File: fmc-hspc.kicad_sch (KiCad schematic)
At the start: 36 parts, among them J18 ASP-184329-01_mounting_holes_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

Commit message: Loclib
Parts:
- C296: footprint antmicro-footprints:0402-cap_EIA -> K410T-devboard-footprints:0402-cap_EIA; symbol antmicroCapacitors0402:C_100n_0402_EIA -> K410T-devboard:C_100n_0402_EIA
- C297: footprint antmicro-footprints:1206-cap -> K410T-devboard-footprints:1206-cap; symbol antmicroCapacitorsmisc:C_47u_16V_1206 -> K410T-devboard:C_47u_16V_1206
- C298, C299, C300, C301, C302, C303, C304, C305, C306, C307, C308, C309, C310, C311, C312, C313: footprint antmicro-footprints:0402-cap -> K410T-devboard-footprints:0402-cap; symbol antmicroCapacitors0402:C_100n_0402 -> K410T-devboard:C_100n_0402
- D32: footprint antmicro-footprints:Nexperia_SOD128 -> K410T-devboard-footprints:Nexperia_SOD128; symbol antmicroDiodesRectifiersSingle:PMEG3050EP,115 -> K410T-devboard:PMEG3050EP,115
- J18: footprint antmicro-footprints:ASP-184329-01_mounting_holes -> K410T-devboard-footprints:ASP-184329-01_mounting_holes; symbol antmicroFMC+Connectors:ASP-184329-01_mounting_holes_FMCPinout -> K410T-devboard:ASP-184329-01_mounting_holes_FMCPinout
- R264: footprint antmicro-footprints:0402-res -> K410T-devboard-footprints:0402-res; symbol antmicroResistors0402:R_100k_0402 -> K410T-devboard:R_100k_0402
- R265, R266: footprint antmicro-footprints:0402-res -> K410T-devboard-footprints:0402-res; symbol antmicroResistors0402:R_10k_0402 -> K410T-devboard:R_10k_0402
- R267, R268: footprint antmicro-footprints:0402-res -> K410T-devboard-footprints:0402-res; symbol antmicroResistors0402:R_4k7_0402 -> K410T-devboard:R_4k7_0402
- R269, R270, R271, R272, R273, R274, R275, R276: footprint antmicro-footprints:0402-res -> K410T-devboard-footprints:0402-res; symbol antmicroResistors0402:R_33R_0402 -> K410T-devboard:R_33R_0402
- TP1, TP2, TP3: footprint antmicro-footprints:Testpoint_smd_0_75mm -> K410T-devboard-footprints:Testpoint_smd_0_75mm; symbol antmicroTestPoints:TP_SMD_0_75MM -> K410T-devboard:TP_SMD_0_75MM

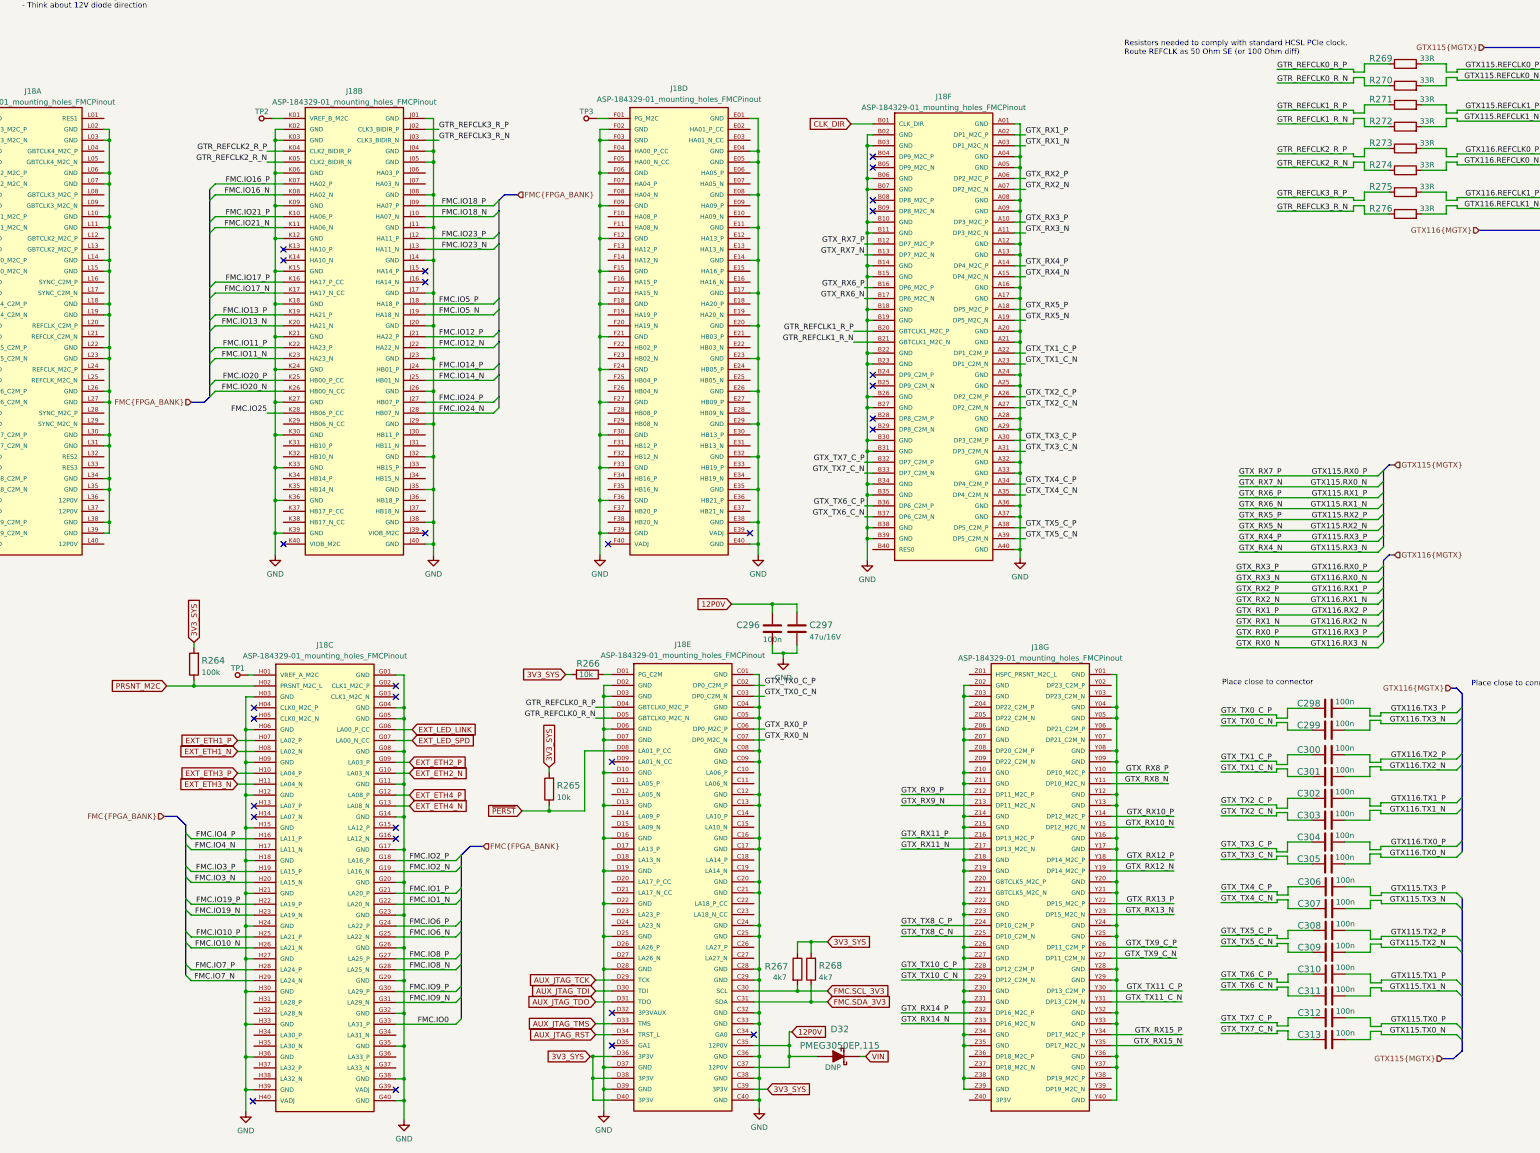
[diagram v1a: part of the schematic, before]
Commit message: Finished FMC signals routing
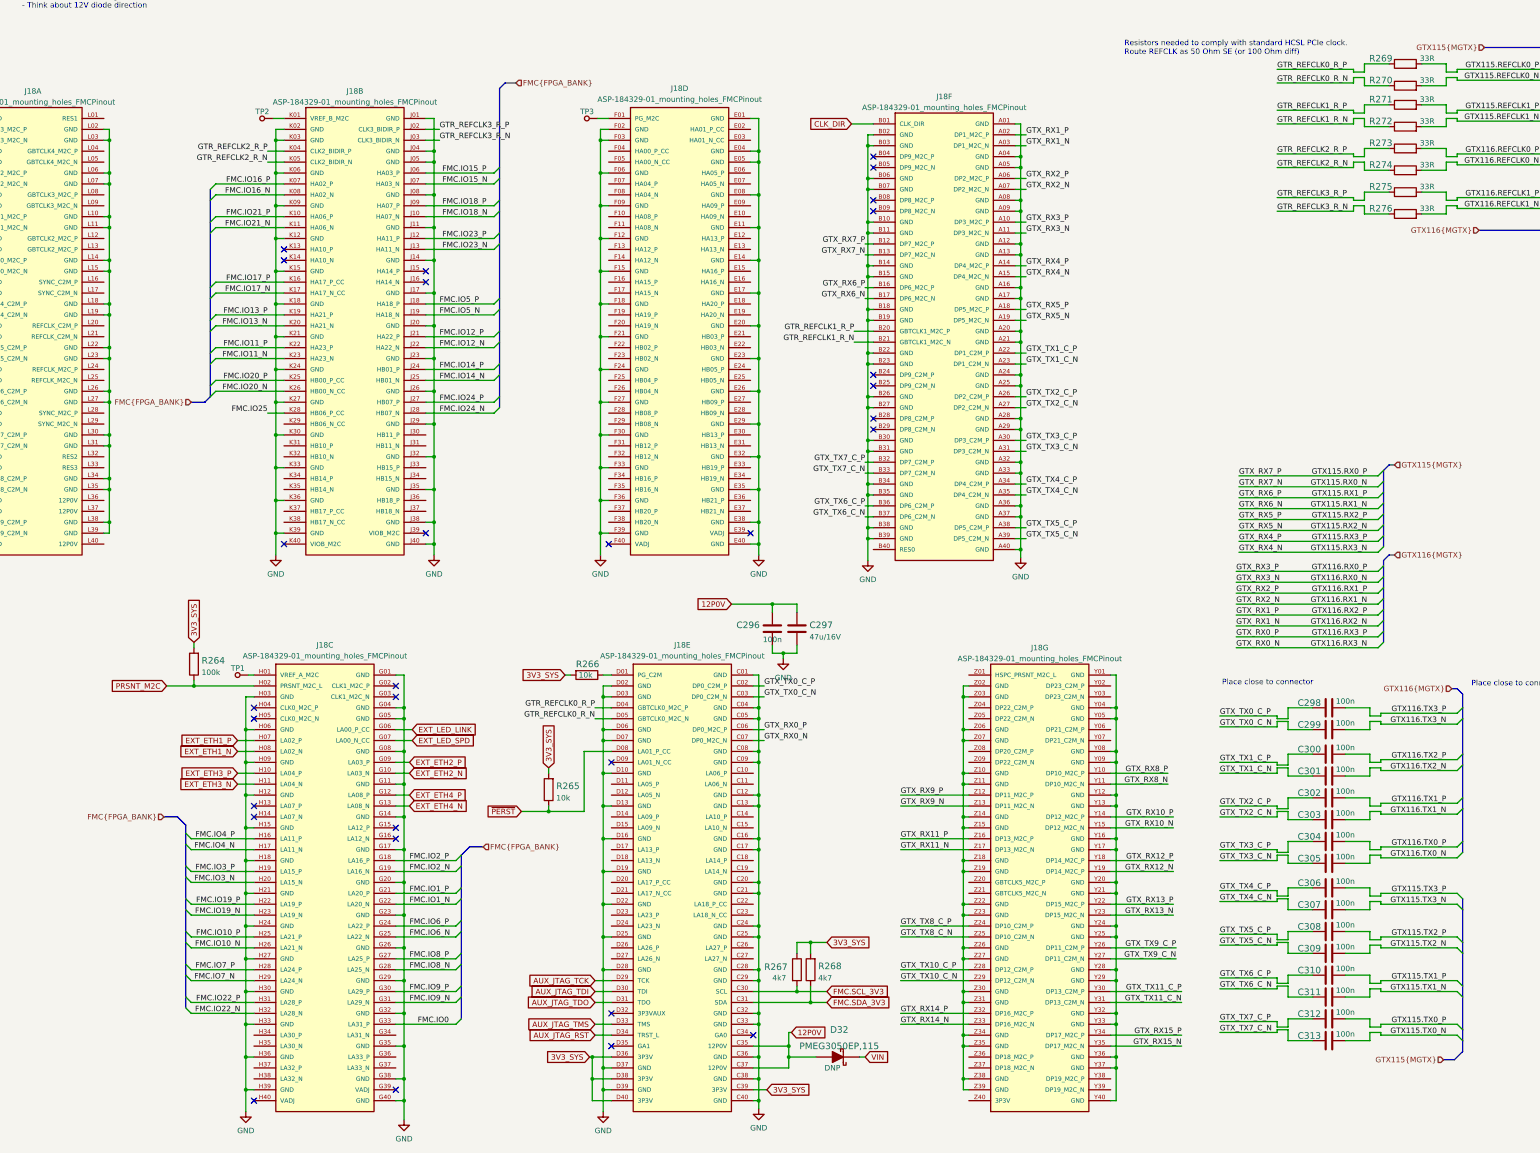
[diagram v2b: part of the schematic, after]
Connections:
- net FMC.IO15_P: now reaches J18.J06 (HA03_P)
- net FMC.IO15_N: now reaches J18.J07 (HA03_N)
- net FMC.IO22_P: now reaches J18.H31 (LA28_P)
- net FMC.IO22_N: now reaches J18.H32 (LA28_N)

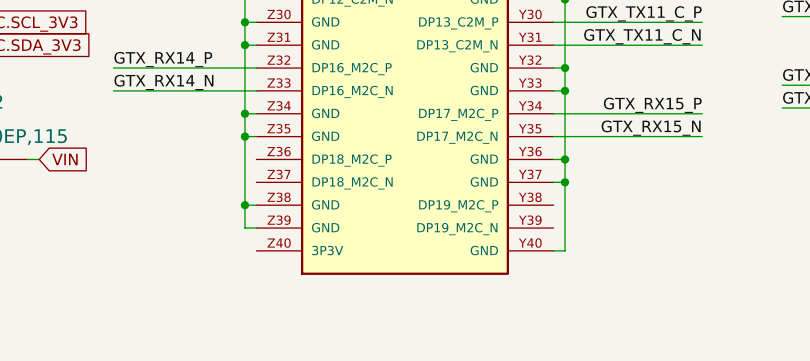
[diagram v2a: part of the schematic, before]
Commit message: Add missing GND connections
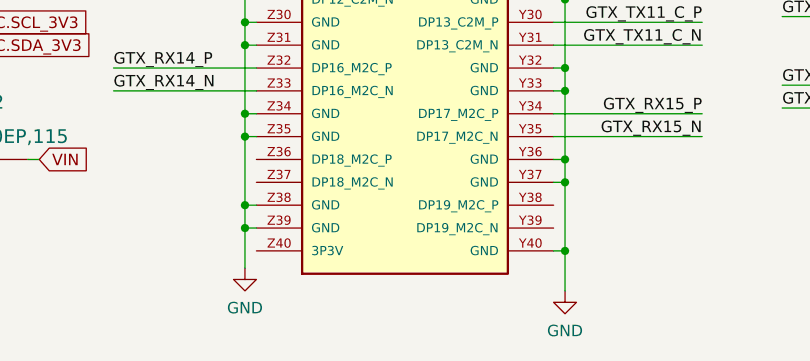
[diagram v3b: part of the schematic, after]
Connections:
- net GND: now also J18.Y01 (GND), J18.Y04 (GND), J18.Y05 (GND), J18.Y08 (GND), J18.Y09 (GND), J18.Y12 (GND), J18.Y13 (GND), J18.Y16 (GND), J18.Y17 (GND), J18.Y20 (GND), J18.Y21 (GND), J18.Y24 (GND), J18.Y25 (GND), J18.Y28 (GND), J18.Y29 (GND), J18.Y32 (GND), J18.Y33 (GND), J18.Y36 (GND), J18.Y37 (GND), J18.Y40 (GND), J18.Z02 (GND), J18.Z03 (GND), J18.Z06 (GND), J18.Z07 (GND), J18.Z10 (GND), J18.Z11 (GND), J18.Z14 (GND), J18.Z15 (GND), J18.Z18 (GND), J18.Z19 (GND), J18.Z22 (GND), J18.Z23 (GND), J18.Z26 (GND), J18.Z27 (GND), J18.Z30 (GND), J18.Z31 (GND), J18.Z34 (GND), J18.Z35 (GND), J18.Z38 (GND), J18.Z39 (GND)
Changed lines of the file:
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@@
   (junction (at 297.18 219.71) (diameter 0) (color 0 0 0 0)
   )
+  (junction (at 261.62 257.81) (diameter 0) (color 0 0 0 0)
+  )
   (junction (at 297.18 250.19) (diameter 0) (color 0 0 0 0)
   )
@@
   (junction (at 131.445 171.45) (diameter 0) (color 0 0 0 0)
   )
+  (junction (at 297.18 260.35) (diameter 0) (color 0 0 0 0)
+  )
   (junction (at 239.395 58.42) (diameter 0) (color 0 0 0 0)
   )
@@
     (stroke (width 0) (type default) (color 0 0 0 0))
   )
+  (wire (pts (xy 297.18 260.35) (xy 297.18 264.795))
+    (stroke (width 0) (type default) (color 0 0 0 0))
+  )
   (wire (pts (xy 273.685 111.76) (xy 274.955 111.76))
     (stroke (width 0) (type default) (color 0 0 0 0))
@@
     (stroke (width 0) (type default) (color 0 0 0 0))
   )
+  (wire (pts (xy 261.62 257.81) (xy 261.62 262.255))
+    (stroke (width 0) (type default) (color 0 0 0 0))
+  )
   (wire (pts (xy 358.775 242.57) (xy 358.775 243.205))
     (stroke (width 0) (type default) (color 0 0 0 0))
@@
     (pin "1")
   )
+  (symbol (lib_id "K410T-devboard:GND") (at 261.62 262.255 0) (unit 1)
+    (in_bom yes) (on_board yes) (fields_autoplaced)
+    (property "Reference" "#PWR?" (id 0) (at 261.62 268.605 0)
+      (effects (font (size 1.27 1.27)) hide)
+    )
+    (property "Value" "GND" (id 1) (at 261.62 266.6984 0))
+    (property "Footprint" "" (id 2) (at 261.62 262.255 0)
+      (effects (font (size 1.27 1.27)) hide)
+    )
+    (property "Datasheet" "" (id 3) (at 261.62 262.255 0)
+      (effects (font (size 1.27 1.27)) hide)
+    )
+    (pin "1")
+  )
   (symbol (lib_id "K410T-devboard:GND") (at 219.71 157.48 0) (unit 1)
     (in_bom yes) (on_board yes) (fields_autoplaced)
@@
     (pin "2")
   )
+  (symbol (lib_id "K410T-devboard:GND") (at 297.18 264.795 0) (unit 1)
+    (in_bom yes) (on_board yes) (fields_autoplaced)
+    (property "Reference" "#PWR?" (id 0) (at 297.18 271.145 0)
+      (effects (font (size 1.27 1.27)) hide)
+    )
+    (property "Value" "GND" (id 1) (at 297.18 269.2384 0))
+    (property "Footprint" "" (id 2) (at 297.18 264.795 0)
+      (effects (font (size 1.27 1.27)) hide)
+    )
+    (property "Datasheet" "" (id 3) (at 297.18 264.795 0)
+      (effects (font (size 1.27 1.27)) hide)
+    )
+    (pin "1")
+  )
   (symbol (lib_id "K410T-devboard:C_100n_0402") (at 346.71 231.14 90) (unit 1)

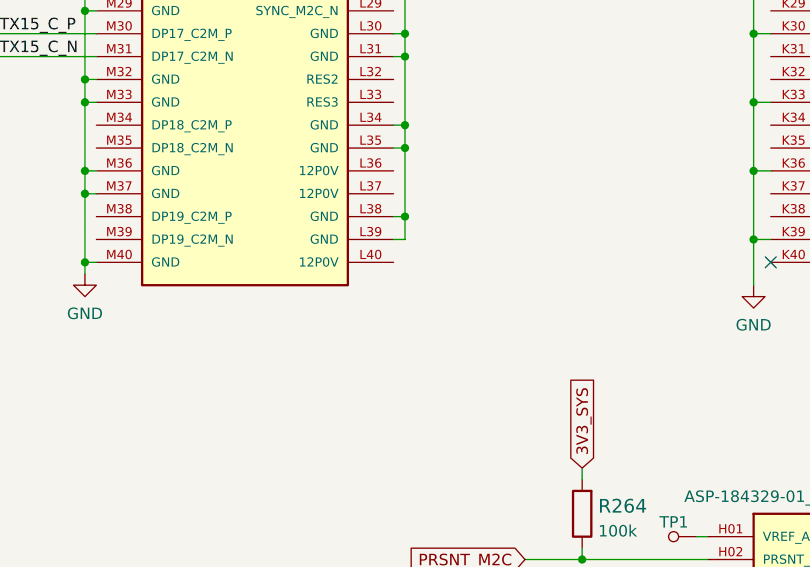
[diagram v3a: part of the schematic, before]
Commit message: Add missing GND connection to FMC L row
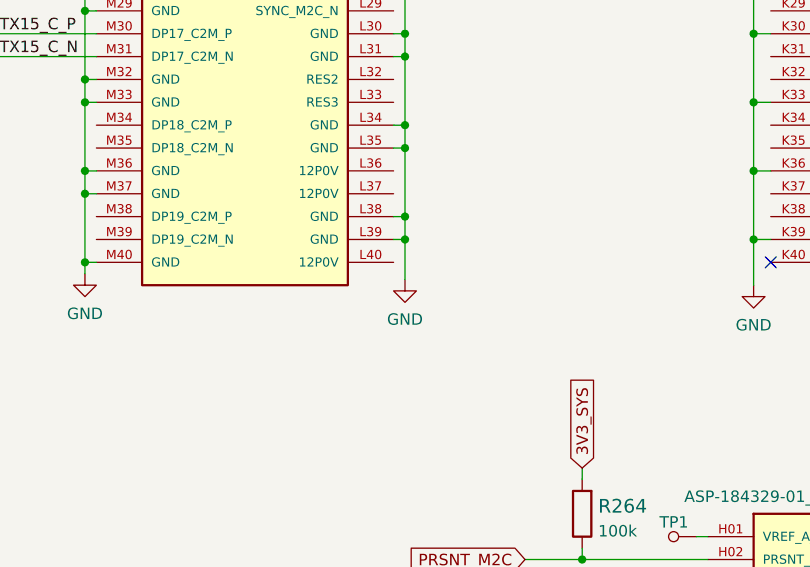
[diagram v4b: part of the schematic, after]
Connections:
- net GND: now also J18.L02 (GND), J18.L03 (GND), J18.L06 (GND), J18.L07 (GND), J18.L10 (GND), J18.L11 (GND), J18.L14 (GND), J18.L15 (GND), J18.L18 (GND), J18.L19 (GND), J18.L22 (GND), J18.L23 (GND), J18.L26 (GND), J18.L27 (GND), J18.L30 (GND), J18.L31 (GND), J18.L34 (GND), J18.L35 (GND), J18.L38 (GND), J18.L39 (GND)
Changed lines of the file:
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@@
   (junction (at 226.06 237.49) (diameter 0) (color 0 0 0 0)
   )
+  (junction (at 62.865 128.27) (diameter 0) (color 0 0 0 0)
+  )
   (junction (at 177.8 184.15) (diameter 0) (color 0 0 0 0)
   )
@@
     (stroke (width 0) (type default) (color 0 0 0 0))
   )
+  (wire (pts (xy 62.865 128.27) (xy 62.865 132.715))
+    (stroke (width 0) (type default) (color 0 0 0 0))
+  )
   (bus (pts (xy 153.67 88.9) (xy 153.67 91.44))
     (stroke (width 0) (type default) (color 0 0 0 0))
@@
     (pin "2")
   )
+  (symbol (lib_id "K410T-devboard:GND") (at 62.865 132.715 0) (unit 1)
+    (in_bom yes) (on_board yes) (fields_autoplaced)
+    (property "Reference" "#PWR?" (id 0) (at 62.865 139.065 0)
+      (effects (font (size 1.27 1.27)) hide)
+    )
+    (property "Value" "GND" (id 1) (at 62.865 137.1584 0))
+    (property "Footprint" "" (id 2) (at 62.865 132.715 0)
+      (effects (font (size 1.27 1.27)) hide)
+    )
+    (property "Datasheet" "" (id 3) (at 62.865 132.715 0)
+      (effects (font (size 1.27 1.27)) hide)
+    )
+    (pin "1")
+  )
   (symbol (lib_id "K410T-devboard:GND") (at 274.955 133.985 0) (unit 1)

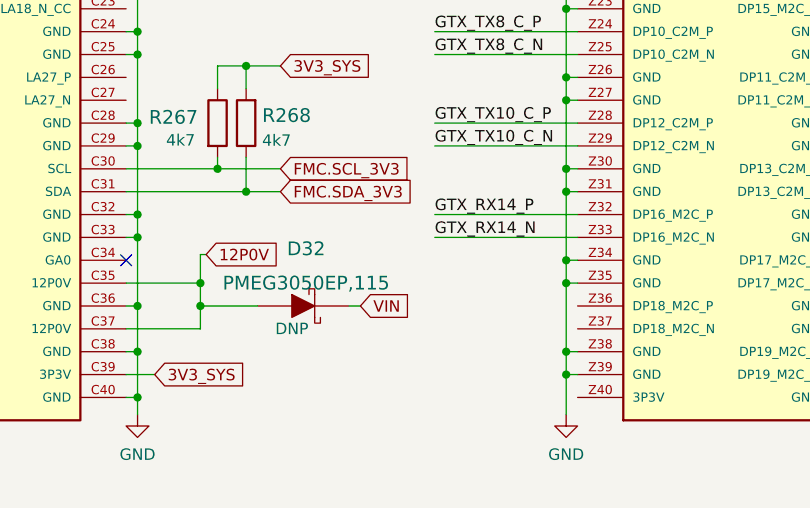
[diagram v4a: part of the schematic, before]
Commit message: Connect FMC 12V diode to VDC instead of VIN
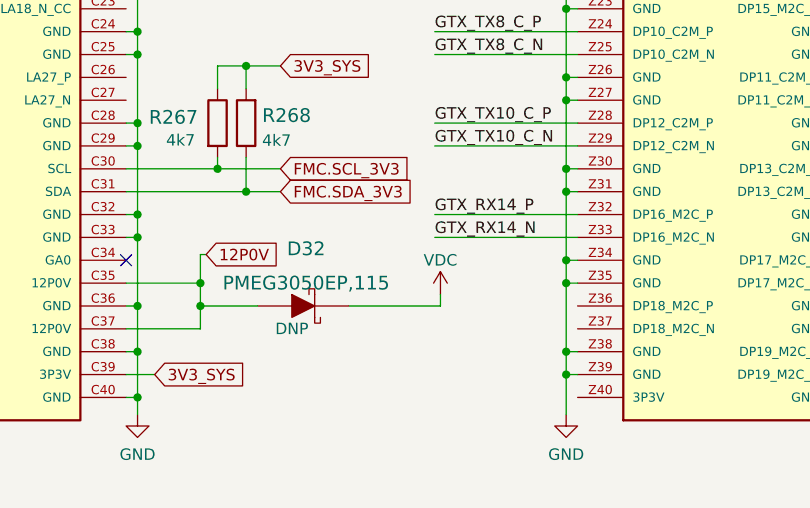
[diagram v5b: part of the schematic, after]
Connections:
- net VIN renamed VDC
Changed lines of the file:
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@@
     (stroke (width 0) (type default) (color 0 0 0 0))
   )
+  (wire (pts (xy 247.65 248.92) (xy 247.65 250.19))
+    (stroke (width 0) (type default) (color 0 0 0 0))
+  )
   (bus (pts (xy 359.41 135.89) (xy 359.41 138.43))
     (stroke (width 0) (type default) (color 0 0 0 0))
@@
     (stroke (width 0) (type default) (color 0 0 0 0))
   )
-  (wire (pts (xy 238.76 250.19) (xy 237.49 250.19))
+  (wire (pts (xy 237.49 250.19) (xy 247.65 250.19))
     (stroke (width 0) (type default) (color 0 0 0 0))
   )
@@
     )
   )
-  (global_label "VIN" (shape input) (at 238.76 250.19 0) (fields_autoplaced)
-    (effects (font (size 1.27 1.27)) (justify left))
-    (property "Intersheet References" "${INTERSHEET_REFS}" (id 0) (at 244.108 250.1106 0)
-      (effects (font (size 1.27 1.27)) (justify left) hide)
-    )
-  )
   (hierarchical_label "FMC{FPGA_BANK}" (shape input) (at 75.565 194.31 180)
     (effects (font (size 1.27 1.27)) (justify right))
@@
   (symbol (lib_id "K410T-devboard:GND") (at 261.62 262.255 0) (unit 1)
     (in_bom yes) (on_board yes) (fields_autoplaced)
-    (property "Reference" "#PWR?" (id 0) (at 261.62 268.605 0)
+    (property "Reference" "#PWR0478" (id 0) (at 261.62 268.605 0)
       (effects (font (size 1.27 1.27)) hide)
     )
@@
     (pin "1")
   )
+  (symbol (lib_id "K410T-devboard:VDC") (at 247.65 248.92 0) (unit 1)
+    (in_bom yes) (on_board yes)
+    (property "Reference" "#PWR?" (id 0) (at 247.65 251.46 0)
+      (effects (font (size 1.27 1.27)) hide)
+    )
+    (property "Value" "VDC" (id 1) (at 247.65 245.11 0))
+    (property "Footprint" "" (id 2) (at 247.65 248.92 0)
+      (effects (font (size 1.27 1.27)) hide)
+    )
+    (property "Datasheet" "" (id 3) (at 247.65 248.92 0)
+      (effects (font (size 1.27 1.27)) hide)
+    )
+    (pin "1")
+  )
   (symbol (lib_id "K410T-devboard:GND") (at 219.71 157.48 0) (unit 1)
     (in_bom yes) (on_board yes) (fields_autoplaced)
@@
   (symbol (lib_id "K410T-devboard:GND") (at 62.865 132.715 0) (unit 1)
     (in_bom yes) (on_board yes) (fields_autoplaced)
-    (property "Reference" "#PWR?" (id 0) (at 62.865 139.065 0)
+    (property "Reference" "#PWR0479" (id 0) (at 62.865 139.065 0)
       (effects (font (size 1.27 1.27)) hide)
     )
@@
   (symbol (lib_id "K410T-devboard:GND") (at 297.18 264.795 0) (unit 1)
     (in_bom yes) (on_board yes) (fields_autoplaced)
-    (property "Reference" "#PWR?" (id 0) (at 297.18 271.145 0)
+    (property "Reference" "#PWR0477" (id 0) (at 297.18 271.145 0)
       (effects (font (size 1.27 1.27)) hide)
     )
